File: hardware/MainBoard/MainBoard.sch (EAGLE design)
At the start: 15 parts, among them J1 CON-71439-2164, J2 CON-71741-2184-TOP, J3 CON-FTSH-105-01-L-DV-K, J4 CON-ZX62R-B-5P, U1 A2F500M3G-FG256, U2 MAX19706-T4877-4, U3 MAX19706-T4877-4, U4 USBLC6-2SC6, U5 FT232HL, X1 CON-SMA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

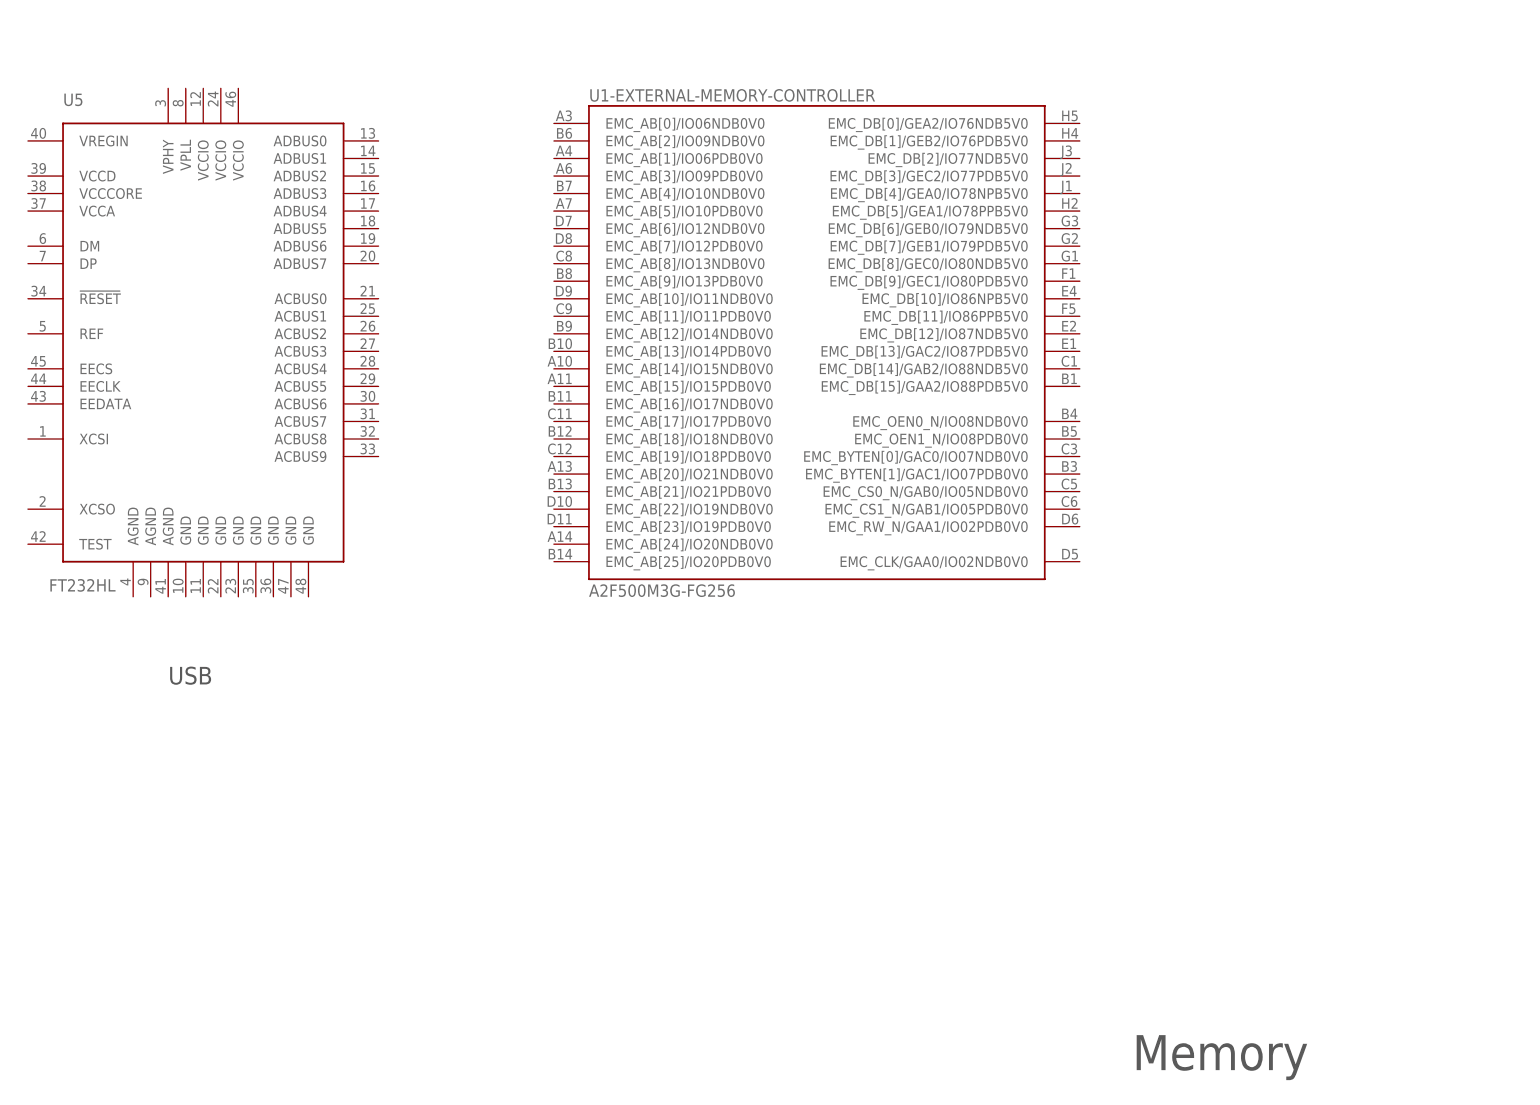
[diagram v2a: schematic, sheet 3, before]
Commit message: Updated pinout spreadsheet and added Ethernet Phy device to library.
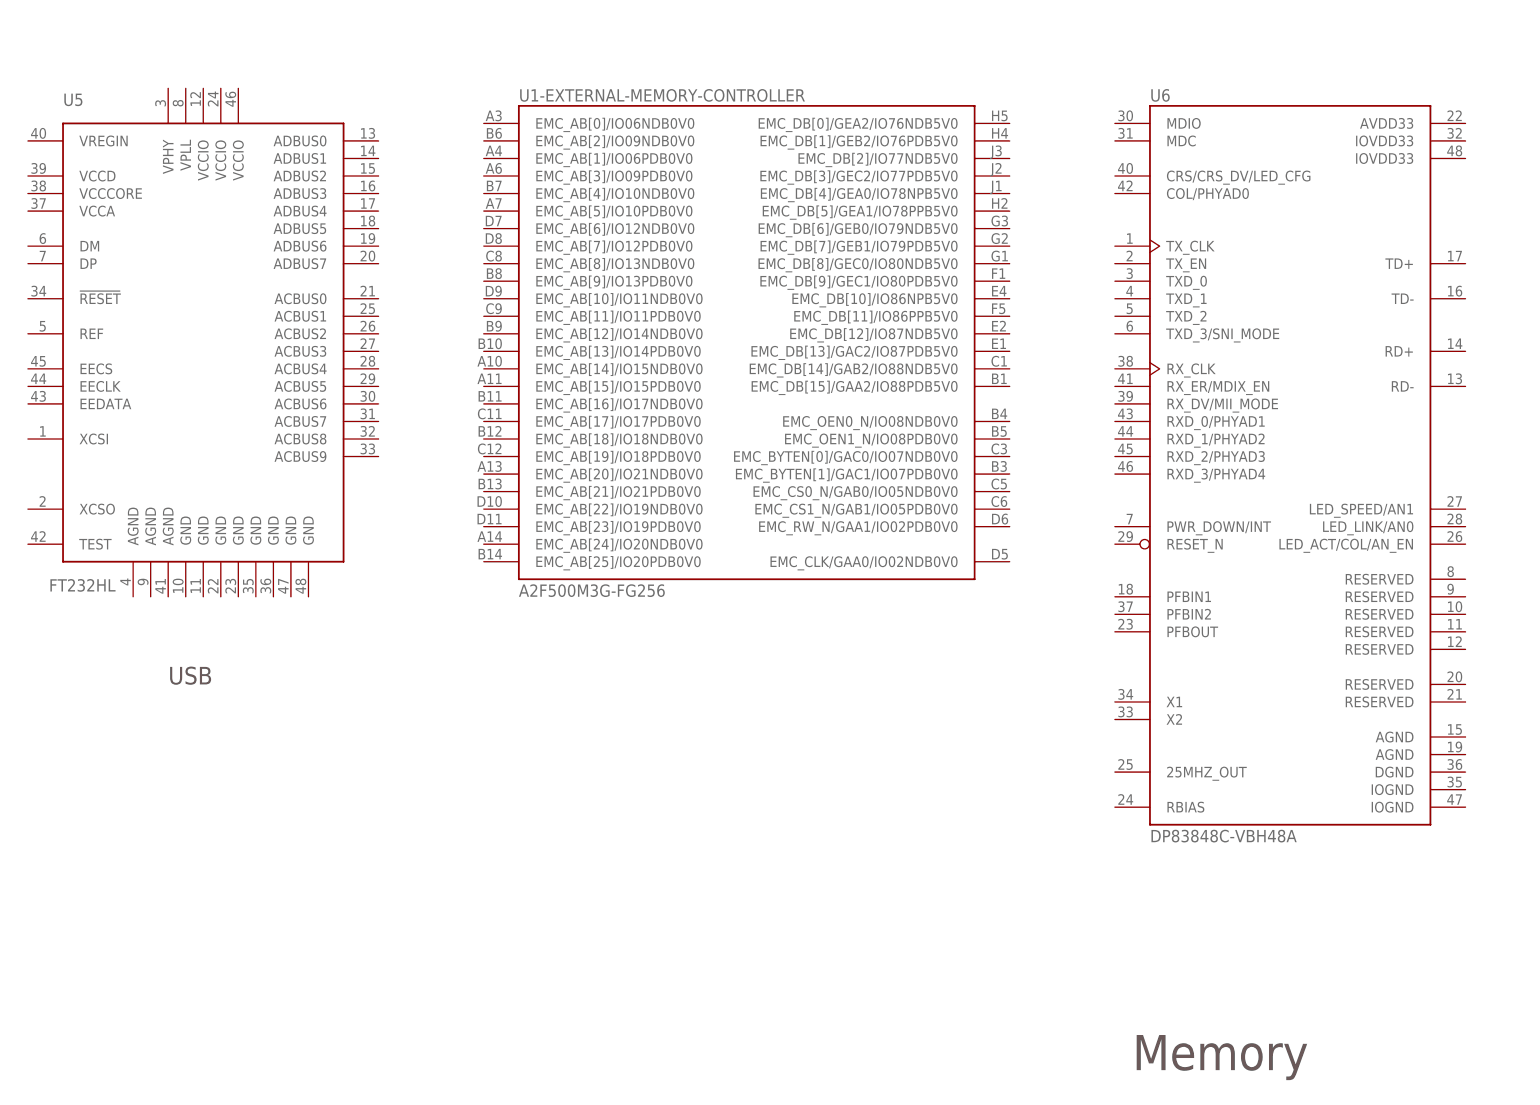
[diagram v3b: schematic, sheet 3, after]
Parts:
- added U6: DP83848C-VBH48A, MainBoard:DP83848C-VBH48A
- U5: MPN (none) -> 768-1101-1-ND
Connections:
- new net ADC1+: J2.62, U2-ADC-DAC.IAP
- new net ADC1-: J2.60, U2-ADC-DAC.IAN
- new net ADC2+: J2.56, U2-ADC-DAC.QAP
- new net ADC2-: J2.54, U2-ADC-DAC.QAN
- new net DAC1+: J2.74, U2-ADC-DAC.QDP
- new net DAC1-: J2.72, U2-ADC-DAC.QDN
- new net DAC2+: J2.68, U2-ADC-DAC.IDP
- new net DAC2-: J2.66, U2-ADC-DAC.IDN
- new net N$13: U3-ADC-DAC.QAP
- new net N$15: U3-ADC-DAC.QAN
- new net N$16: U3-ADC-DAC.IDP
- new net N$17: U3-ADC-DAC.IDN
- new net N$18: U3-ADC-DAC.QDP
- new net N$19: U3-ADC-DAC.QDN
- new net N$8: U3-ADC-DAC.IAP
- new net N$9: U3-ADC-DAC.IAN
- net AGND: now also J2.52, J2.58, J2.64, J2.70
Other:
- moved on the sheet: U1-EXTERNAL-MEMORY-CONTROLLER, U2-ADC-DAC, U3-ADC-DAC
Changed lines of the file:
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@@
 <part name="PORT13" library="MainBoard" deviceset="PORT5" device=""/>
 <part name="PORT14" library="MainBoard" deviceset="PORT5" device=""/>
-<part name="U5" library="MainBoard" deviceset="FT232H" device="L"/>
+<part name="U5" library="MainBoard" deviceset="FT232H" device="L">
+<attribute name="MPN" value="768-1101-1-ND"/>
+</part>
 <part name="U2" library="MainBoard" deviceset="MAX19706" device="-T4877-4"/>
 <part name="U3" library="MainBoard" deviceset="MAX19706" device="-T4877-4"/>
@@
 <part name="PORT27" library="MainBoard" deviceset="PORT5" device=""/>
 <part name="PORT28" library="MainBoard" deviceset="PORT5" device=""/>
+<part name="U6" library="MainBoard" deviceset="DP83848C" device="-VBH48A"/>
+<part name="PORT29" library="MainBoard" deviceset="PORT5" device=""/>
+<part name="PORT30" library="MainBoard" deviceset="PORT5" device=""/>
+<part name="PORT31" library="MainBoard" deviceset="PORT5" device=""/>
+<part name="PORT32" library="MainBoard" deviceset="PORT5" device=""/>
+<part name="PORT33" library="MainBoard" deviceset="PORT5" device=""/>
+<part name="PORT34" library="MainBoard" deviceset="PORT5" device=""/>
+<part name="PORT35" library="MainBoard" deviceset="PORT5" device=""/>
+<part name="PORT36" library="MainBoard" deviceset="PORT5" device=""/>
 </parts>
 <sheets>
@@
 <instance part="FRAME7" gate="G$1" x="0" y="0"/>
 <instance part="FRAME7" gate="G$2" x="147.32" y="0"/>
-<instance part="U1" gate="-EXTERNAL-MEMORY-CONTROLLER" x="147.32" y="127"/>
+<instance part="U1" gate="-EXTERNAL-MEMORY-CONTROLLER" x="137.16" y="127"/>
 <instance part="U5" gate="G$1" x="58.42" y="127"/>
+<instance part="U6" gate="G$1" x="215.9" y="111.76"/>
 </instances>
 <busses>
@@
 <instance part="FRAME4" gate="G$1" x="0" y="0"/>
 <instance part="FRAME4" gate="G$2" x="147.32" y="0"/>
-<instance part="U2" gate="-ADC-DAC" x="226.06" y="142.24"/>
-<instance part="U3" gate="-ADC-DAC" x="190.5" y="76.2"/>
+<instance part="U2" gate="-ADC-DAC" x="58.42" y="137.16"/>
+<instance part="U3" gate="-ADC-DAC" x="58.42" y="53.34"/>
 </instances>
 <busses>
 </busses>
 <nets>
+<net name="ADC2+" class="0">
+<segment>
+<label x="22.86" y="157.48" size="1.778" layer="95"/>
+<pinref part="U2" gate="-ADC-DAC" pin="QAP"/>
+<wire x1="33.02" y1="157.48" x2="43.18" y2="157.48" width="0.1524" layer="91"/>
+</segment>
+</net>
+<net name="ADC2-" class="0">
+<segment>
+<label x="22.86" y="152.4" size="1.778" layer="95"/>
+<pinref part="U2" gate="-ADC-DAC" pin="QAN"/>
+<wire x1="43.18" y1="152.4" x2="33.02" y2="152.4" width="0.1524" layer="91"/>
+</segment>
+</net>
+<net name="ADC1+" class="0">
+<segment>
+<label x="22.86" y="170.18" size="1.778" layer="95"/>
+<pinref part="U2" gate="-ADC-DAC" pin="IAP"/>
+<wire x1="43.18" y1="170.18" x2="33.02" y2="170.18" width="0.1524" layer="91"/>
+</segment>
+</net>
+<net name="ADC1-" class="0">
+<segment>
+<label x="22.86" y="165.1" size="1.778" layer="95"/>
+<pinref part="U2" gate="-ADC-DAC" pin="IAN"/>
+<wire x1="33.02" y1="165.1" x2="43.18" y2="165.1" width="0.1524" layer="91"/>
+</segment>
+</net>
+<net name="N$8" class="0">
+<segment>
+<pinref part="U3" gate="-ADC-DAC" pin="IAP"/>
+<wire x1="43.18" y1="86.36" x2="33.02" y2="86.36" width="0.1524" layer="91"/>
+</segment>
+</net>
+<net name="N$9" class="0">
+<segment>
+<pinref part="U3" gate="-ADC-DAC" pin="IAN"/>
+<wire x1="43.18" y1="81.28" x2="33.02" y2="81.28" width="0.1524" layer="91"/>
+</segment>
+</net>
+<net name="N$13" class="0">
+<segment>
+<pinref part="U3" gate="-ADC-DAC" pin="QAP"/>
+<wire x1="43.18" y1="73.66" x2="33.02" y2="73.66" width="0.1524" layer="91"/>
+</segment>
+</net>
+<net name="N$15" class="0">
+<segment>
+<pinref part="U3" gate="-ADC-DAC" pin="QAN"/>
+<wire x1="43.18" y1="68.58" x2="33.02" y2="68.58" width="0.1524" layer="91"/>
+</segment>
+</net>
+<net name="N$16" class="0">
+<segment>
+<pinref part="U3" gate="-ADC-DAC" pin="IDP"/>
+<wire x1="43.18" y1="58.42" x2="33.02" y2="58.42" width="0.1524" layer="91"/>
+</segment>
+</net>
+<net name="N$17" class="0">
+<segment>
+<pinref part="U3" gate="-ADC-DAC" pin="IDN"/>
+<wire x1="43.18" y1="53.34" x2="33.02" y2="53.34" width="0.1524" layer="91"/>
+</segment>
+</net>
+<net name="N$18" class="0">
+<segment>
+<pinref part="U3" gate="-ADC-DAC" pin="QDP"/>
+<wire x1="43.18" y1="45.72" x2="33.02" y2="45.72" width="0.1524" layer="91"/>
+</segment>
+</net>
+<net name="N$19" class="0">
+<segment>
+<pinref part="U3" gate="-ADC-DAC" pin="QDN"/>
+<wire x1="43.18" y1="40.64" x2="33.02" y2="40.64" width="0.1524" layer="91"/>
+</segment>
+</net>
+<net name="DAC2+" class="0">
+<segment>
+<pinref part="U2" gate="-ADC-DAC" pin="IDP"/>
+<wire x1="43.18" y1="142.24" x2="33.02" y2="142.24" width="0.1524" layer="91"/>
+<label x="22.86" y="142.24" size="1.778" layer="95"/>
+</segment>
+</net>
+<net name="DAC2-" class="0">
+<segment>
+<pinref part="U2" gate="-ADC-DAC" pin="IDN"/>
+<wire x1="43.18" y1="137.16" x2="33.02" y2="137.16" width="0.1524" layer="91"/>
+<label x="22.86" y="137.16" size="1.778" layer="95"/>
+</segment>
+</net>
+<net name="DAC1+" class="0">
+<segment>
+<pinref part="U2" gate="-ADC-DAC" pin="QDP"/>
+<wire x1="43.18" y1="129.54" x2="33.02" y2="129.54" width="0.1524" layer="91"/>
+<label x="22.86" y="129.54" size="1.778" layer="95"/>
+</segment>
+</net>
+<net name="DAC1-" class="0">
+<segment>
+<pinref part="U2" gate="-ADC-DAC" pin="QDN"/>
+<wire x1="43.18" y1="124.46" x2="33.02" y2="124.46" width="0.1524" layer="91"/>
+<label x="22.86" y="124.46" size="1.778" layer="95"/>
+</segment>
+</net>
 </nets>
 </sheet>
@@
 <instance part="PORT27" gate="G$1" x="228.6" y="63.5"/>
 <instance part="PORT28" gate="G$1" x="228.6" y="60.96"/>
+<instance part="PORT29" gate="G$1" x="228.6" y="71.12"/>
+<instance part="PORT30" gate="G$1" x="228.6" y="73.66"/>
+<instance part="PORT31" gate="G$1" x="228.6" y="78.74"/>
+<instance part="PORT32" gate="G$1" x="228.6" y="81.28"/>
+<instance part="PORT33" gate="G$1" x="228.6" y="86.36"/>
+<instance part="PORT34" gate="G$1" x="228.6" y="88.9"/>
+<instance part="PORT35" gate="G$1" x="228.6" y="93.98"/>
+<instance part="PORT36" gate="G$1" x="228.6" y="96.52"/>
 </instances>
 <busses>
@@
 <junction x="210.82" y="58.42"/>
 <pinref part="U$16" gate="G$1" pin="AGND"/>
-</segment>
-</net>
+<pinref part="J2" gate="G$1" pin="70"/>
+<wire x1="208.28" y1="76.2" x2="210.82" y2="76.2" width="0.1524" layer="91"/>
+<wire x1="210.82" y1="76.2" x2="210.82" y2="68.58" width="0.1524" layer="91"/>
+<pinref part="J2" gate="G$1" pin="64"/>
+<wire x1="208.28" y1="83.82" x2="210.82" y2="83.82" width="0.1524" layer="91"/>
+<wire x1="210.82" y1="83.82" x2="210.82" y2="76.2" width="0.1524" layer="91"/>
+<pinref part="J2" gate="G$1" pin="58"/>
+<wire x1="208.28" y1="91.44" x2="210.82" y2="91.44" width="0.1524" layer="91"/>
+<wire x1="210.82" y1="91.44" x2="210.82" y2="83.82" width="0.1524" layer="91"/>
+<pinref part="J2" gate="G$1" pin="52"/>
+<wire x1="208.28" y1="99.06" x2="210.82" y2="99.06" width="0.1524" layer="91"/>
+<wire x1="210.82" y1="99.06" x2="210.82" y2="91.44" width="0.1524" layer="91"/>
+<junction x="210.82" y="68.58"/>
+<junction x="210.82" y="76.2"/>
+<junction x="210.82" y="83.82"/>
+<junction x="210.82" y="91.44"/>
+</segment>
+</net>
+<net name="DAC1+" class="0">
+<segment>
+<pinref part="J2" gate="G$1" pin="74"/>
+<wire x1="208.28" y1="71.12" x2="218.44" y2="71.12" width="0.1524" layer="91"/>
+<label x="220.98" y="71.12" size="1.778" layer="95"/>
+</segment>
+</net>
+<net name="DAC1-" class="0">
+<segment>
+<pinref part="J2" gate="G$1" pin="72"/>
+<wire x1="208.28" y1="73.66" x2="218.44" y2="73.66" width="0.1524" layer="91"/>
+<label x="220.98" y="73.66" size="1.778" layer="95"/>
+</segment>
+</net>
+<net name="DAC2+" class="0">
+<segment>
+<pinref part="J2" gate="G$1" pin="68"/>
+<wire x1="208.28" y1="78.74" x2="218.44" y2="78.74" width="0.1524" layer="91"/>
+<label x="220.98" y="78.74" size="1.778" layer="95"/>
+</segment>
+</net>
+<net name="DAC2-" class="0">
+<segment>
+<pinref part="J2" gate="G$1" pin="66"/>
+<wire x1="208.28" y1="81.28" x2="218.44" y2="81.28" width="0.1524" layer="91"/>
+<label x="220.98" y="81.28" size="1.778" layer="95"/>
+</segment>
+</net>
+<net name="ADC1+" class="0">
+<segment>
+<pinref part="J2" gate="G$1" pin="62"/>
+<wire x1="208.28" y1="86.36" x2="218.44" y2="86.36" width="0.1524" layer="91"/>
+<label x="220.98" y="86.36" size="1.778" layer="95"/>
+</segment>
+</net>
+<net name="ADC1-" class="0">
+<segment>
+<pinref part="J2" gate="G$1" pin="60"/>
+<wire x1="208.28" y1="88.9" x2="218.44" y2="88.9" width="0.1524" layer="91"/>
+<label x="220.98" y="88.9" size="1.778" layer="95"/>
+</segment>
+</net>
+<net name="ADC2+" class="0">
+<segment>
+<pinref part="J2" gate="G$1" pin="56"/>
+<wire x1="208.28" y1="93.98" x2="218.44" y2="93.98" width="0.1524" layer="91"/>
+<label x="220.98" y="93.98" size="1.778" layer="95"/>
+</segment>
+</net>
+<net name="ADC2-" class="0">
+<segment>
+<pinref part="J2" gate="G$1" pin="54"/>
+<wire x1="208.28" y1="96.52" x2="218.44" y2="96.52" width="0.1524" layer="91"/>
+<label x="220.98" y="96.52" size="1.778" layer="95"/>
+</segment>
+</net>

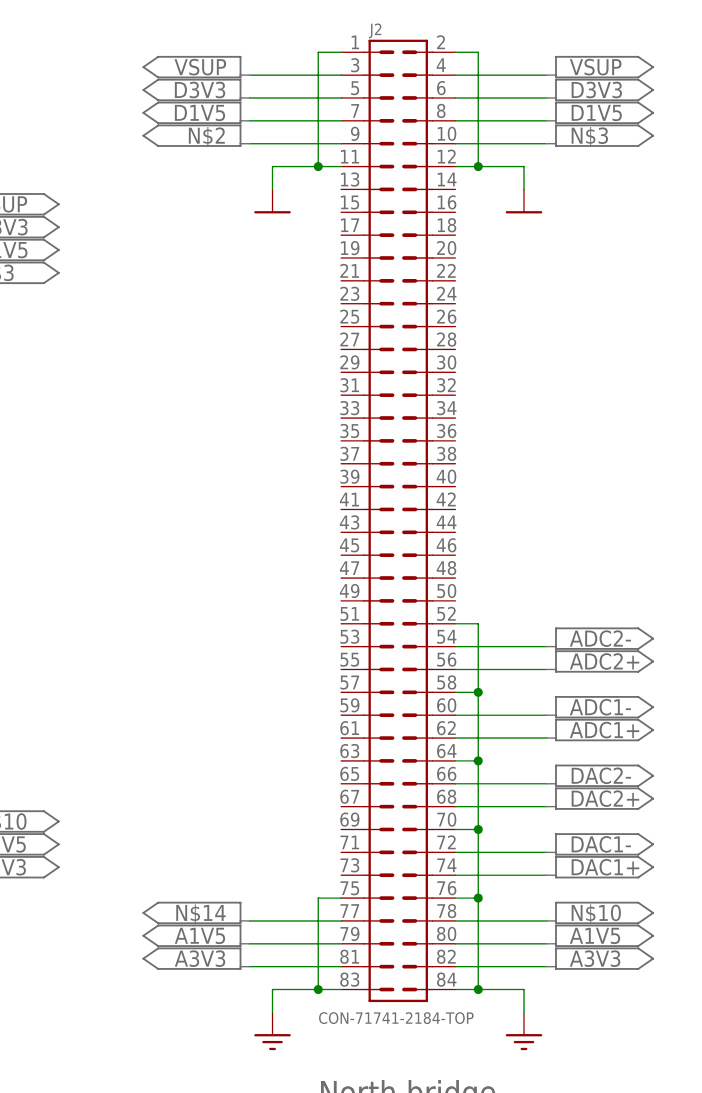
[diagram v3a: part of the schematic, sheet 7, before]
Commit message: Finalized upper connector (North Bridge) high-speed analog (ADC and DAC) signal pinout.
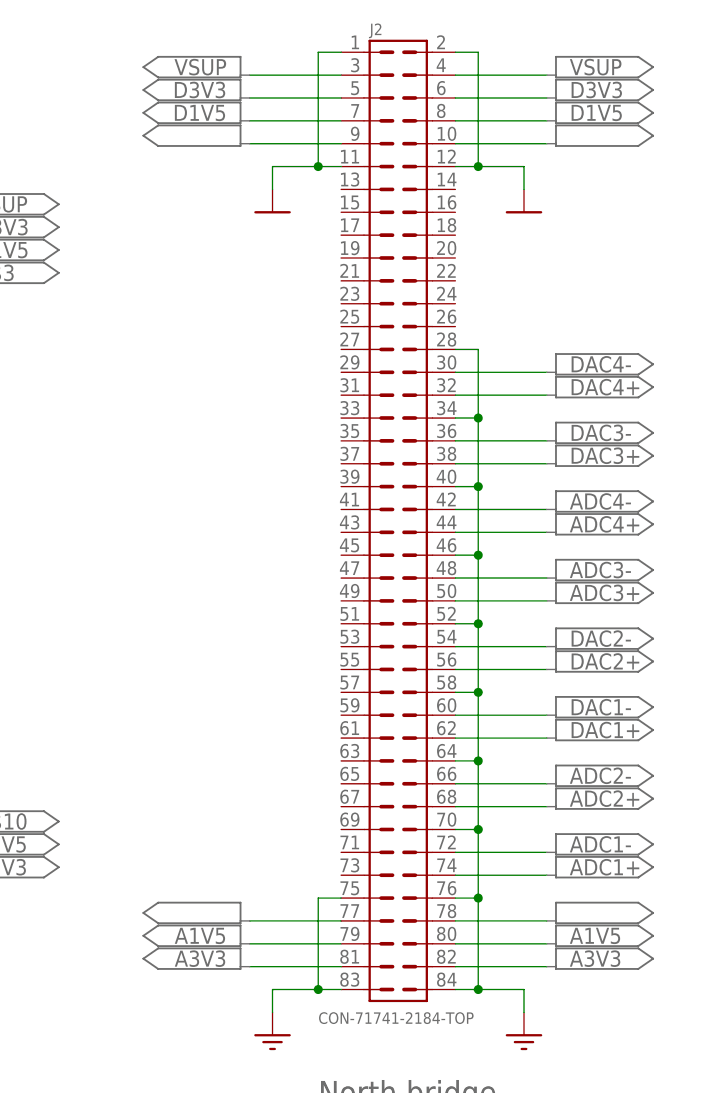
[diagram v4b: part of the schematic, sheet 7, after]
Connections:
- removed net N$13: U3-ADC-DAC.QAP
- removed net N$15: U3-ADC-DAC.QAN
- removed net N$16: U3-ADC-DAC.IDP
- removed net N$17: U3-ADC-DAC.IDN
- removed net N$18: U3-ADC-DAC.QDP
- removed net N$19: U3-ADC-DAC.QDN
- removed net N$8: U3-ADC-DAC.IAP
- removed net N$9: U3-ADC-DAC.IAN
- new net ADC3+: J2.50, U3-ADC-DAC.QAP
- new net ADC3-: J2.48, U3-ADC-DAC.QAN
- new net ADC4+: J2.44, U3-ADC-DAC.IAP
- new net ADC4-: J2.42, U3-ADC-DAC.IAN
- new net DAC3+: J2.38, U3-ADC-DAC.QDP
- new net DAC3-: J2.36, U3-ADC-DAC.QDN
- new net DAC4+: J2.32, U3-ADC-DAC.IDP
- new net DAC4-: J2.30, U3-ADC-DAC.IDN
- net ADC1+: now also J2.74, U2-ADC-DAC.QAP; no longer J2.62, U2-ADC-DAC.IAP
- net ADC1-: now also J2.72, U2-ADC-DAC.QAN; no longer J2.60, U2-ADC-DAC.IAN
- net ADC2+: now also J2.68, U2-ADC-DAC.IAP; no longer J2.56, U2-ADC-DAC.QAP
- net ADC2-: now also J2.66, U2-ADC-DAC.IAN; no longer J2.54, U2-ADC-DAC.QAN
- net AGND: now also J2.28, J2.34, J2.40, J2.46
- net DAC1+: now also J2.62; no longer J2.74
- net DAC1-: now also J2.60; no longer J2.72
- net DAC2+: now also J2.56; no longer J2.68
- net DAC2-: now also J2.54; no longer J2.66

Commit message: Added oscillator and crystal components to library and updated 'Clocks' sheet on schematic.
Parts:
- added C1, C2: 10pF, MainBoard:C0603
- added C3, C4: 4pF, MainBoard:C0603
- added J5, J6: CON-SMA, MainBoard:CON-SMA
- added R1, R2: 39, MainBoard:R0603
- added X3: ECX-31B, MainBoard:ECX-31B
- added X4: ASEM1, MainBoard:ASEM1
- X1: value CON-SMA -> FOX924B; device MainBoard:CON-SMA -> MainBoard:FOX924B
- X2: value CON-SMA -> ECX-2236-200; device MainBoard:CON-SMA -> MainBoard:ECX-2236-200
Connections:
- new net EXT_CLK_IN: J5G1.A
- new net EXT_CLK_OUT: J6G1.A
- new net MAC_EN: U6.RESET_N, X4.OE
- new net MSS_RMII_CLK: R1.2
- new net N$1: C4.1, U1-MISC.LPXOUT, X3.1
- new net N$5: C3.1, U1-MISC.LPXIN, X3.2
- new net N$6: C2.1, U1-MISC.MAINXOUT, X2.1
- new net N$7: C1.1, U1-MISC.MAINXIN, X2.2
- new net N$8: X1.FO
- new net PHY_RMII_CLK: R2.2, U6.X1
- new net RMII_CLK: R1.1, R2.1, X4.FO
- net A3V3: now also X1.VCC, X4.VDD
- net AGND: now also X1.GND, X4.GND
- net DGND: now also C1.2, C2.2, C3.2, C4.2
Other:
- note added: "Ethernet"
- note added: "NC"
- note removed: "MISC"
